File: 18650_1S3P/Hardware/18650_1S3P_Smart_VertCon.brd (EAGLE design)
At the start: 109.2 x 70 mm, 75 parts, among them J1 CONN_3MICROFIT_RT, J2 GEMS_POWER_PLUGOUTPUT, Q1 AON7522E, Q2 AON7522E, Q3 AON7522E, Q4 AON7522E, Q5 AON7522E, Q6 AON7522E, Q7 DMP2008, Q8 DMP2008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

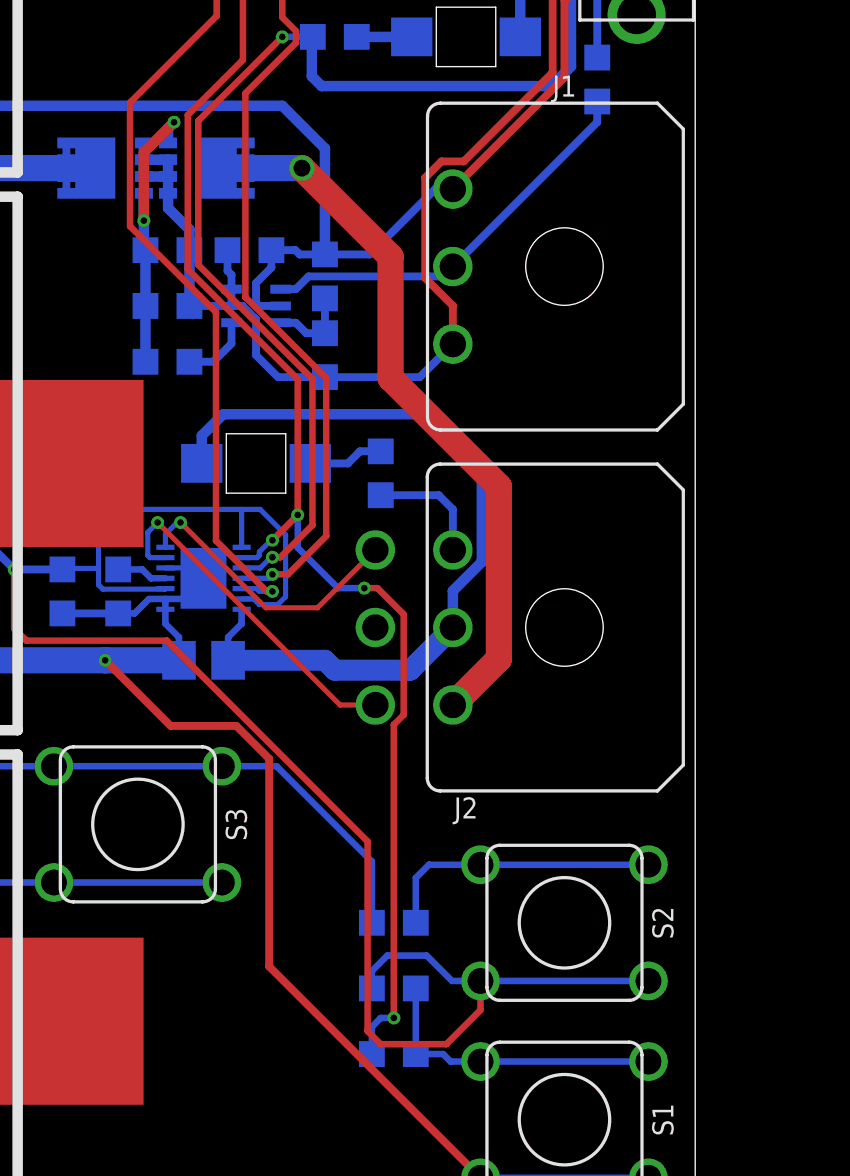
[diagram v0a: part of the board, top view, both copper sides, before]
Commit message: Added 18650_1S3P_Smart v1.2 (very and normal)
Added v1.2 updates for both systems
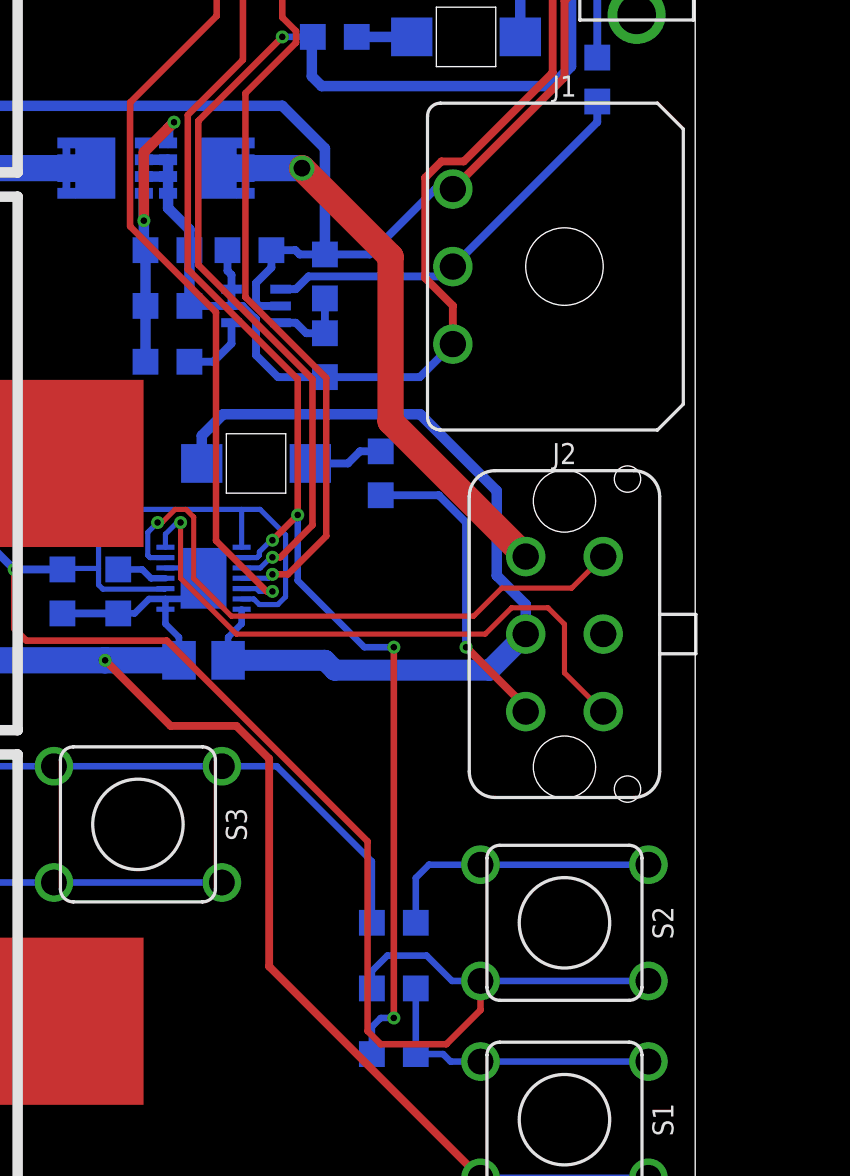
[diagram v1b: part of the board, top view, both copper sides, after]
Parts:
- J2: device bschulz:2X3_MICROFIT_RT -> bschulz:2X3_MICROFIT
- moved J2 0.25 mm to (104.1, 28.4), turned to 270 degrees
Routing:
- net SCL: track 11.1 -> 23.9 mm
- net SDA: track 13.5 -> 23.7 mm
- net N$38: track 4.59 -> 12.0 mm, vias 0 -> 1
- net SYS+: track 31.2 -> 25.1 mm
- net SYS-: track 31.5 -> 34.5 mm
- net LED1: track 80.7 -> 80.1 mm
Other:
- board text added: "1S3P - Smart - 18650 Project Gonk Bobby Schulz v1.2 - Vert"
- board text removed: "1S3P - Smart - 18650 Project Gonk Bobby Schulz v1.2"

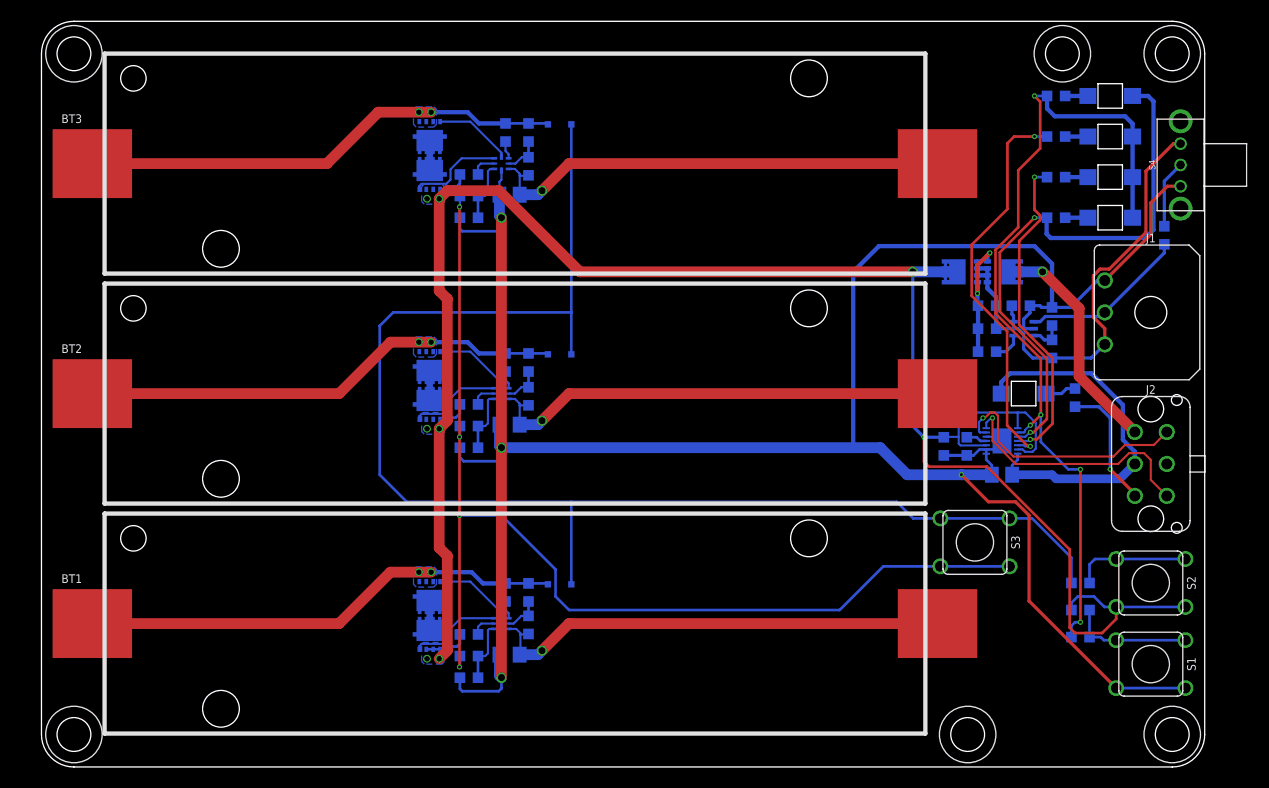
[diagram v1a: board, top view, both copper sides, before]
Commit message: Changed folder structure to include legacy aspects
Also changed 1042P to 1042 to match manufactured version
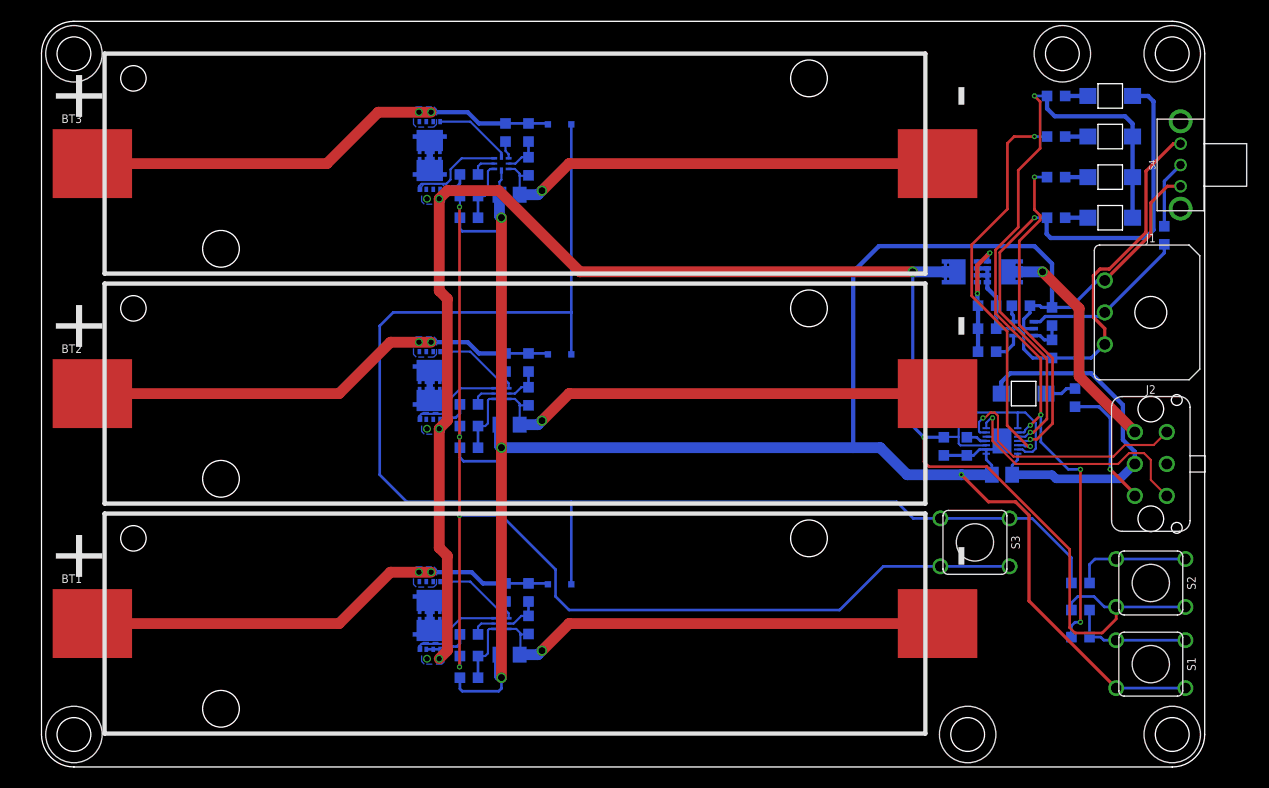
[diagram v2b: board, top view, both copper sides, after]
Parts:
- BT1, BT2, BT3: value 186501042P_NOSILK -> 186501042; device bschulz:BATT_1042P_NOSILK -> bschulz:BATT_1042P
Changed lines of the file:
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@@
 </autorouter>
 <elements>
-<element name="BT1" library="bschulz" package="BATT_1042P_NOSILK" value="186501042P_NOSILK" x="44.45" y="13.462" smashed="yes" rot="R180">
+<element name="BT1" library="bschulz" package="BATT_1042P" value="186501042" x="44.45" y="13.462" smashed="yes" rot="R180">
 <attribute name="DIGIKEY" value="36-1042-ND" x="-13.97" y="24.892" size="1.778" layer="27" rot="R180" display="off"/>
 <attribute name="MF" value="Keystone" x="-13.97" y="24.892" size="1.778" layer="27" rot="R180" display="off"/>
@@
 <attribute name="NAME" x="3.81" y="17.272" size="0.8128" layer="25" font="vector" ratio="15" align="bottom-right"/>
 </element>
-<element name="BT2" library="bschulz" package="BATT_1042P_NOSILK" value="186501042P_NOSILK" x="44.45" y="35.052" smashed="yes" rot="R180">
+<element name="BT2" library="bschulz" package="BATT_1042P" value="186501042" x="44.45" y="35.052" smashed="yes" rot="R180">
 <attribute name="DIGIKEY" value="36-1042-ND" x="-13.97" y="68.072" size="1.778" layer="27" rot="R180" display="off"/>
 <attribute name="MF" value="Keystone" x="-13.97" y="68.072" size="1.778" layer="27" rot="R180" display="off"/>
@@
 <attribute name="NAME" x="3.81" y="38.862" size="0.8128" layer="25" font="vector" ratio="15" align="bottom-right"/>
 </element>
-<element name="BT3" library="bschulz" package="BATT_1042P_NOSILK" value="186501042P_NOSILK" x="44.45" y="56.642" smashed="yes" rot="R180">
+<element name="BT3" library="bschulz" package="BATT_1042P" value="186501042" x="44.45" y="56.642" smashed="yes" rot="R180">
 <attribute name="DIGIKEY" value="36-1042-ND" x="-13.97" y="111.252" size="1.778" layer="27" rot="R180" display="off"/>
 <attribute name="MF" value="Keystone" x="-13.97" y="111.252" size="1.778" layer="27" rot="R180" display="off"/>
@@
 </element>
 <element name="C1" library="bschulz_passives" package="C0603" value="1uF" x="45.72" y="13.335" smashed="yes" rot="MR90">
-<attribute name="DIGIKEY" value="587-1251-1-ND" x="-34.29" y="41.275" size="1.778" layer="28" rot="MR90" display="off"/>
+<attribute name="DIGIKEY" value="587-2984-1-ND" x="-34.29" y="41.275" size="1.778" layer="28" rot="MR90" display="off"/>
 <attribute name="MF" value="Yaiyo Yuden" x="-34.29" y="41.275" size="1.778" layer="28" rot="MR90" display="off"/>
-<attribute name="MPN" value="EMK107BJ105KA-T" x="-34.29" y="41.275" size="1.778" layer="28" rot="MR90" display="off"/>
+<attribute name="MPN" value="TMK107B7105KA-T" x="-34.29" y="41.275" size="1.778" layer="28" rot="MR90" display="off"/>
 <attribute name="NAME" x="46.736" y="13.335" size="0.6096" layer="26" font="vector" ratio="15" rot="MR90" align="center"/>
 <attribute name="VALUE" x="44.323" y="13.335" size="0.6096" layer="28" font="vector" ratio="15" rot="MR90" align="center"/>
 </element>
 <element name="C2" library="bschulz_passives" package="C0603" value="1uF" x="45.72" y="34.798" smashed="yes" rot="MR90">
-<attribute name="DIGIKEY" value="587-1251-1-ND" x="-34.29" y="66.548" size="1.778" layer="28" rot="MR90" display="off"/>
+<attribute name="DIGIKEY" value="587-2984-1-ND" x="-34.29" y="66.548" size="1.778" layer="28" rot="MR90" display="off"/>
 <attribute name="MF" value="Yaiyo Yuden" x="-34.29" y="66.548" size="1.778" layer="28" rot="MR90" display="off"/>
-<attribute name="MPN" value="EMK107BJ105KA-T" x="-34.29" y="66.548" size="1.778" layer="28" rot="MR90" display="off"/>
+<attribute name="MPN" value="TMK107B7105KA-T" x="-34.29" y="66.548" size="1.778" layer="28" rot="MR90" display="off"/>
 <attribute name="NAME" x="46.863" y="34.798" size="0.6096" layer="26" font="vector" ratio="15" rot="MR90" align="center"/>
 <attribute name="VALUE" x="44.323" y="34.798" size="0.6096" layer="28" font="vector" ratio="15" rot="MR90" align="center"/>
 </element>
 <element name="C3" library="bschulz_passives" package="C0603" value="1uF" x="45.72" y="56.388" smashed="yes" rot="MR90">
-<attribute name="DIGIKEY" value="587-1251-1-ND" x="-34.29" y="91.948" size="1.778" layer="28" rot="MR90" display="off"/>
+<attribute name="DIGIKEY" value="587-2984-1-ND" x="-34.29" y="91.948" size="1.778" layer="28" rot="MR90" display="off"/>
 <attribute name="MF" value="Yaiyo Yuden" x="-34.29" y="91.948" size="1.778" layer="28" rot="MR90" display="off"/>
-<attribute name="MPN" value="EMK107BJ105KA-T" x="-34.29" y="91.948" size="1.778" layer="28" rot="MR90" display="off"/>
+<attribute name="MPN" value="TMK107B7105KA-T" x="-34.29" y="91.948" size="1.778" layer="28" rot="MR90" display="off"/>
 <attribute name="NAME" x="46.736" y="56.388" size="0.6096" layer="26" font="vector" ratio="15" rot="MR90" align="center"/>
 <attribute name="VALUE" x="44.323" y="56.388" size="0.6096" layer="28" font="vector" ratio="15" rot="MR90" align="center"/>
@@
 </element>
 <element name="C6" library="bschulz_passives" package="C0603" value="1uF" x="88.773" y="43.307" smashed="yes" rot="MR0">
-<attribute name="DIGIKEY" value="587-1251-1-ND" x="45.593" y="-36.703" size="1.778" layer="28" rot="MR0" display="off"/>
+<attribute name="DIGIKEY" value="587-2984-1-ND" x="45.593" y="-36.703" size="1.778" layer="28" rot="MR0" display="off"/>
 <attribute name="MF" value="Yaiyo Yuden" x="45.593" y="-36.703" size="1.778" layer="28" rot="MR0" display="off"/>
-<attribute name="MPN" value="EMK107BJ105KA-T" x="45.593" y="-36.703" size="1.778" layer="28" rot="MR0" display="off"/>
+<attribute name="MPN" value="TMK107B7105KA-T" x="45.593" y="-36.703" size="1.778" layer="28" rot="MR0" display="off"/>
 <attribute name="NAME" x="89.154" y="44.323" size="0.6096" layer="26" font="vector" ratio="15" rot="MR180" align="center"/>
 <attribute name="VALUE" x="88.773" y="41.91" size="0.6096" layer="28" font="vector" ratio="15" rot="MR0" align="center"/>
@@
 <wire x1="36.576" y1="18.288" x2="40.386" y2="18.288" width="0.4064" layer="16"/>
 <wire x1="40.386" y1="18.288" x2="41.441" y2="17.233" width="0.4064" layer="16"/>
+<wire x1="36.774" y1="17.402" x2="36.124" y2="17.402" width="0" layer="19" extent="16-16"/>
+<wire x1="35.474" y1="17.402" x2="36.124" y2="17.402" width="0" layer="19" extent="16-16"/>
+<wire x1="35.433" y1="18.288" x2="35.474" y2="17.402" width="0" layer="19" extent="16-16"/>
+<wire x1="36.576" y1="18.288" x2="36.774" y2="17.402" width="0" layer="19" extent="16-16"/>
 </signal>
 <signal name="N$7">
@@
 <wire x1="41.06931875" y1="38.823" x2="43.561" y2="38.823" width="0.4064" layer="16"/>
 <wire x1="40.01431875" y1="39.878" x2="41.06931875" y2="38.823" width="0.4064" layer="16"/>
+<wire x1="36.774" y1="38.992" x2="36.124" y2="38.992" width="0" layer="19" extent="16-16"/>
+<wire x1="35.474" y1="38.992" x2="36.124" y2="38.992" width="0" layer="19" extent="16-16"/>
+<wire x1="35.433" y1="39.878" x2="35.474" y2="38.992" width="0" layer="19" extent="16-16"/>
+<wire x1="36.576" y1="39.878" x2="36.774" y2="38.992" width="0" layer="19" extent="16-16"/>
 </signal>
 <signal name="N$16">
@@
 <wire x1="41.06931875" y1="60.413" x2="43.561" y2="60.413" width="0.4064" layer="16"/>
 <wire x1="40.01431875" y1="61.468" x2="41.06931875" y2="60.413" width="0.4064" layer="16"/>
+<wire x1="36.774" y1="60.582" x2="36.124" y2="60.582" width="0" layer="19" extent="16-16"/>
+<wire x1="35.474" y1="60.582" x2="36.124" y2="60.582" width="0" layer="19" extent="16-16"/>
+<wire x1="35.433" y1="61.468" x2="35.474" y2="60.582" width="0" layer="19" extent="16-16"/>
+<wire x1="36.576" y1="61.468" x2="36.774" y2="60.582" width="0" layer="19" extent="16-16"/>
 </signal>
 <signal name="N$25">
